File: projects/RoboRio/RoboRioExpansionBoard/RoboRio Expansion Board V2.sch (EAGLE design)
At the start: 94 parts, among them IC1 FT232RL, J1 RRINTERFACE-FEMALE, J2 MICROSD, Q1 5.0 MHz, T1 NPN-SOT416, T2 NPN-SOT416, U1 P8X32A-Q44, U2 24LC256ST, U4 MC1525TO, U6 RT9193-33GB, U7 RT9193-33GB

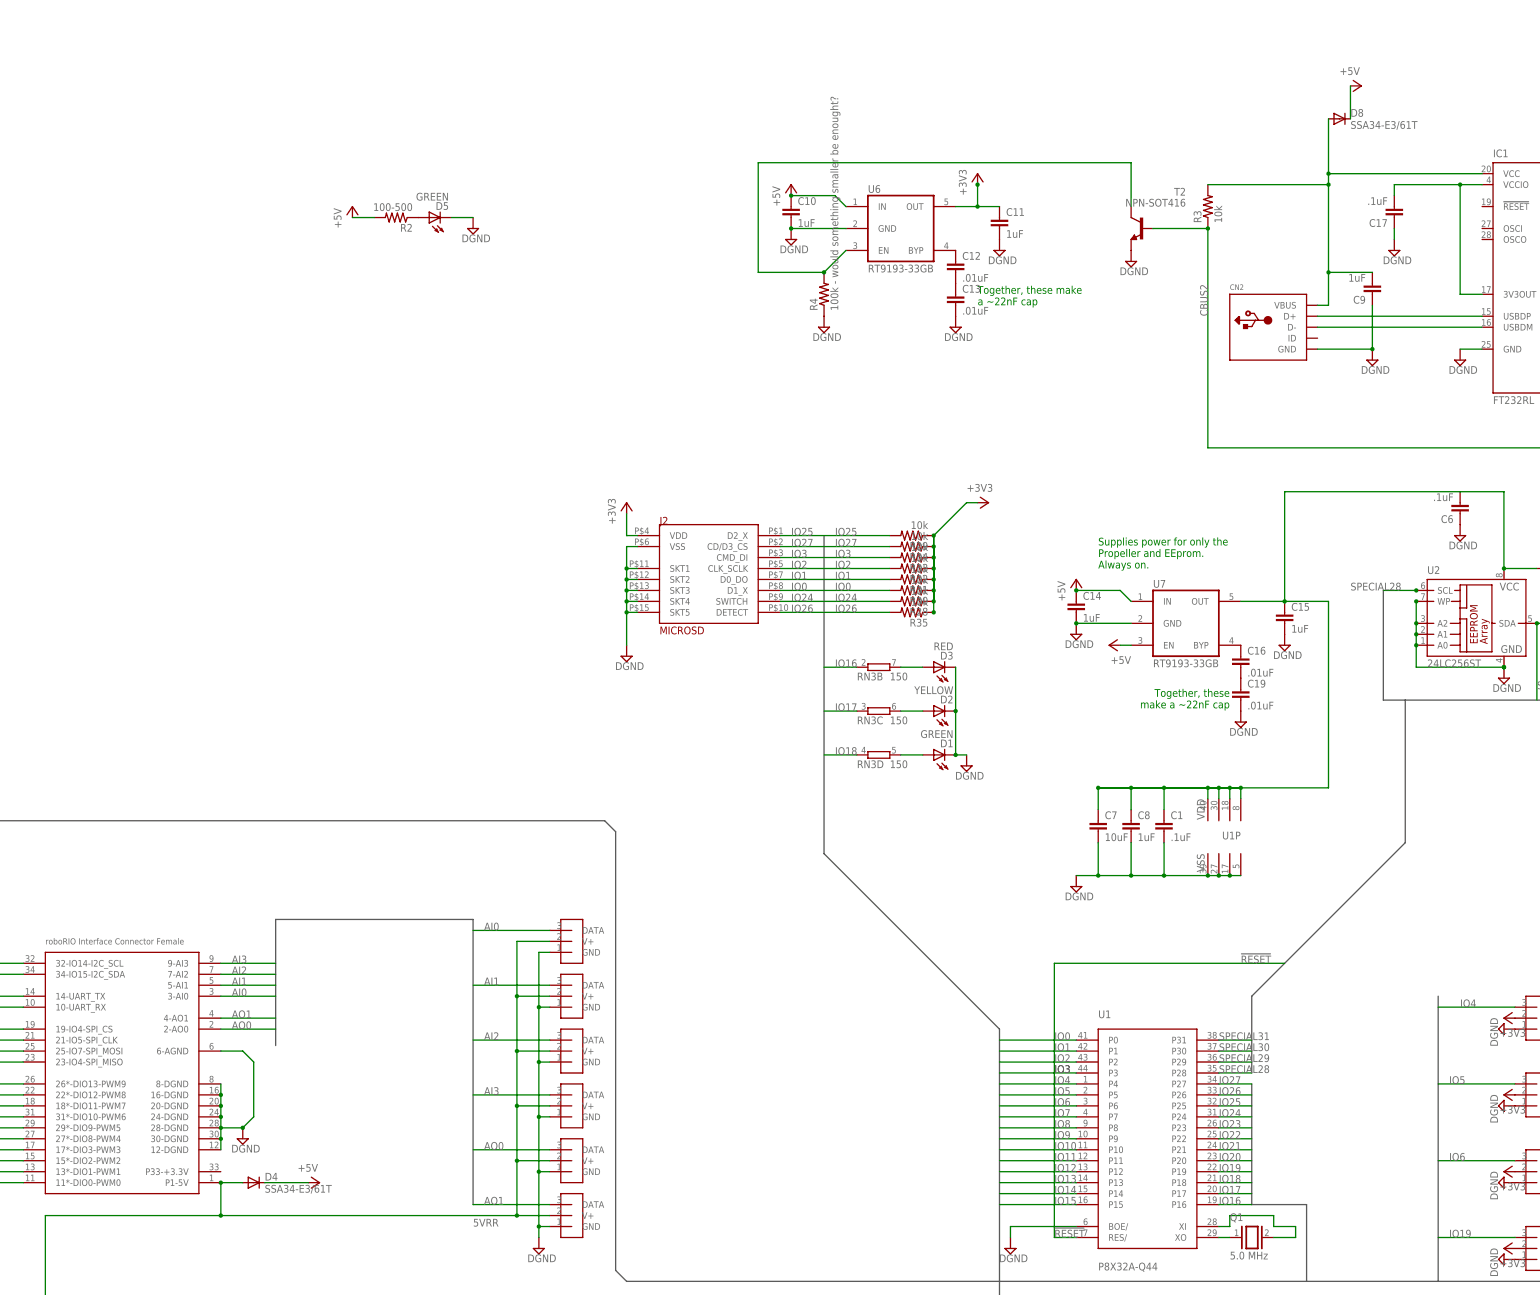
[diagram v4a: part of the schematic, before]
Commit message: Figured out power supply circuit
I think. We need to do a simulation on this!
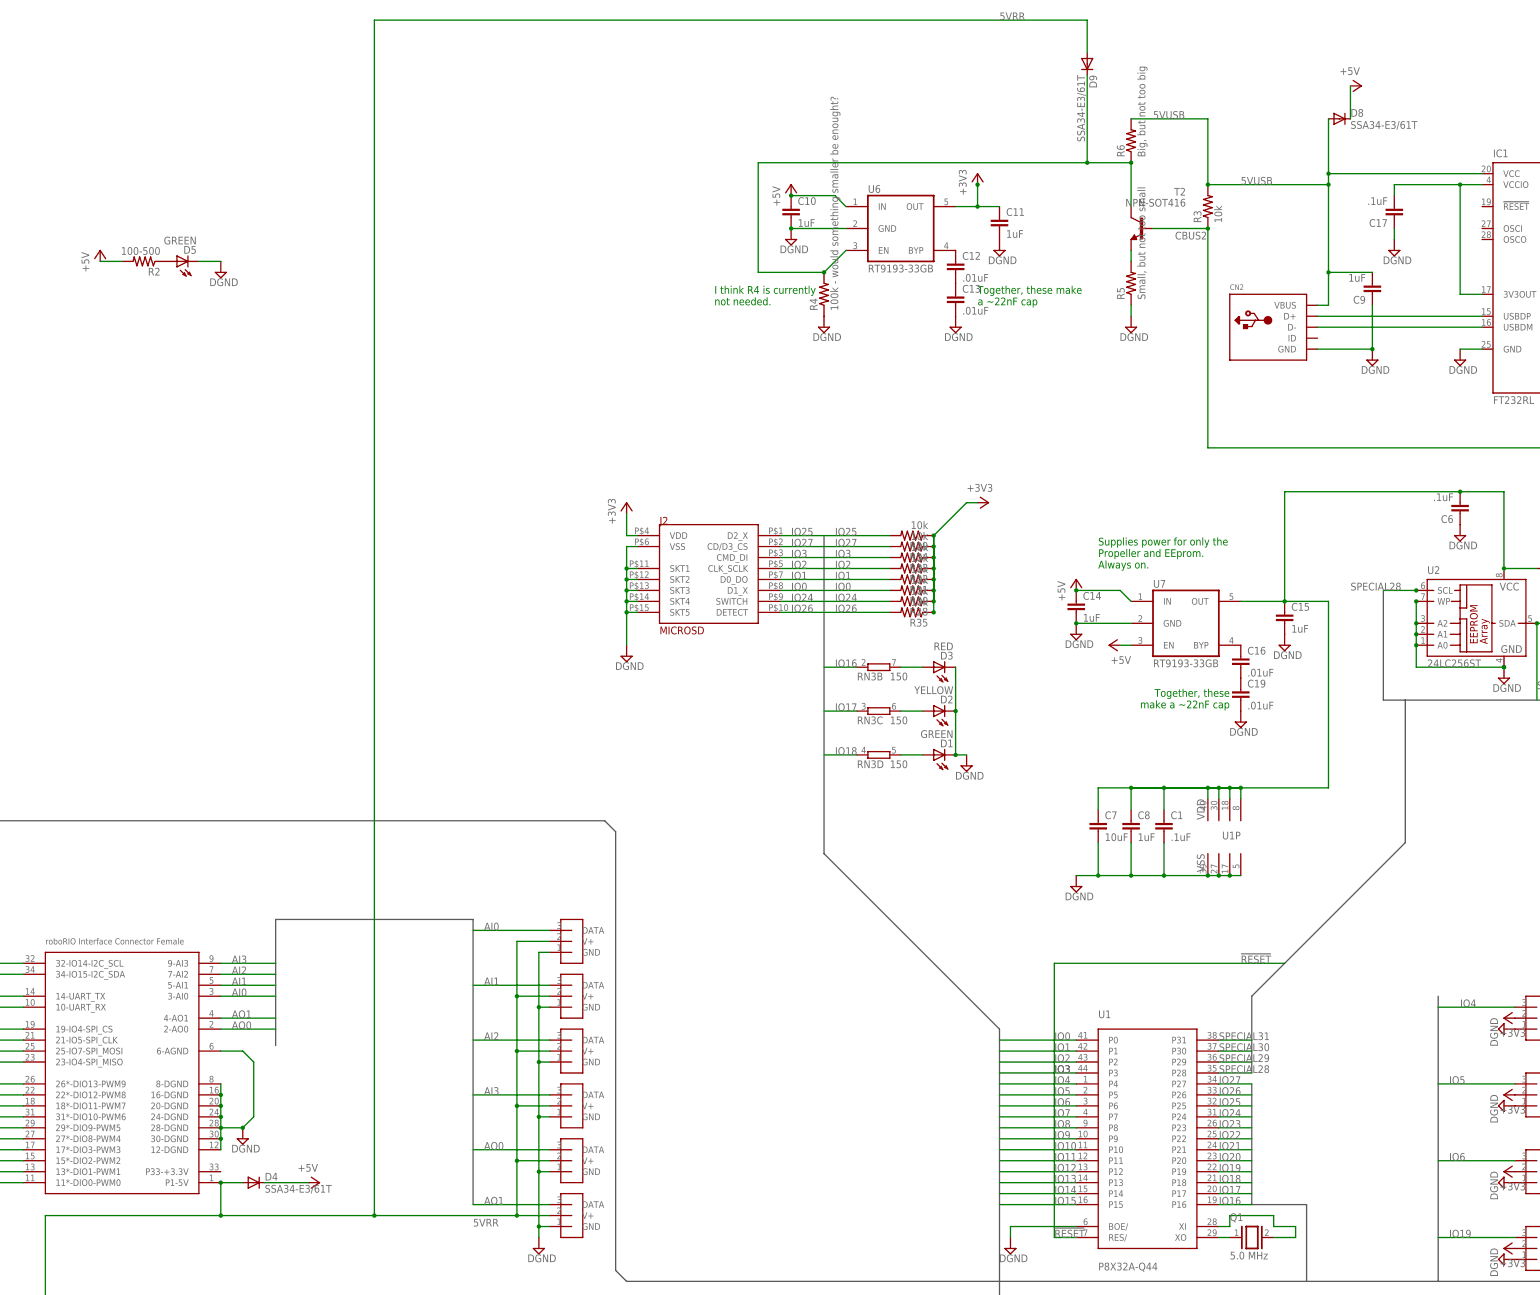
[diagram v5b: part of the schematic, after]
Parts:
- added D9: SSA34-E3/61T, diode:DIODE-DO-214AC
- added R5: Small, but not too small, resistor:R-US_R0603
- added R6: Big, but not too big, resistor:R-US_R0603
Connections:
- new net N$5: R5.2, T2.E
- net 5VRR: now also D9.A
- net 5VUSB: now also R6.2
- net DGND: now also R5.1; no longer T2.E
- net N$25: now also D9.C, R6.1
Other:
- note added: "I think R4 is currently not needed."
- moved on the sheet: D5, R2
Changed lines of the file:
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@@
 <part name="R4" library="resistor" deviceset="R-US_" device="R0603" value="100k - would something smaller be enought?"/>
 <part name="SUPPLY52" library="supply2" deviceset="DGND" device=""/>
+<part name="R5" library="resistor" deviceset="R-US_" device="R0603" value="Small, but not too small"/>
+<part name="D9" library="diode" deviceset="DIODE-" device="DO-214AC" value="SSA34-E3/61T"/>
+<part name="R6" library="resistor" deviceset="R-US_" device="R0603" value="Big, but not too big"/>
 </parts>
 <sheets>
@@
 Propeller and EEprom.
 Always on.</text>
+<text x="-66.04" y="226.06" size="1.778" layer="91">I think R4 is currently
+not needed.</text>
 </plain>
 <instances>
@@
 <instance part="P+13" gate="1" x="254" y="-95.25" rot="R180"/>
 <instance part="P+14" gate="1" x="256.54" y="-72.39" rot="R180"/>
-<instance part="D5" gate="G$1" x="-132.08" y="246.38" rot="R90"/>
-<instance part="SUPPLY39" gate="G$1" x="-121.92" y="243.84"/>
+<instance part="D5" gate="G$1" x="-190.5" y="236.22" rot="R90"/>
+<instance part="SUPPLY39" gate="G$1" x="-180.34" y="233.68"/>
 <instance part="+3V7" gate="G$1" x="-5.08" y="256.54"/>
-<instance part="P+16" gate="1" x="-149.86" y="248.92"/>
+<instance part="P+16" gate="1" x="-208.28" y="238.76"/>
 <instance part="+3V3" gate="G$1" x="116.84" y="60.96" rot="R90"/>
 <instance part="SUPPLY5" gate="G$1" x="116.84" y="58.42" rot="R270"/>
@@
 <instance part="U$36" gate="G$1" x="241.3" y="60.96" rot="R180"/>
 <instance part="U$37" gate="G$1" x="96.52" y="-27.94" rot="R180"/>
-<instance part="R2" gate="G$1" x="-139.7" y="246.38" rot="R180"/>
+<instance part="R2" gate="G$1" x="-198.12" y="236.22" rot="R180"/>
 <instance part="U6" gate="G$1" x="-22.86" y="243.84"/>
 <instance part="C10" gate="G$1" x="-48.26" y="248.92"/>
@@
 <instance part="P+4" gate="1" x="83.82" y="276.86" rot="R270"/>
 <instance part="T2" gate="G$1" x="33.02" y="243.84" rot="MR0"/>
-<instance part="SUPPLY51" gate="G$1" x="30.48" y="236.22"/>
+<instance part="SUPPLY51" gate="G$1" x="30.48" y="220.98"/>
 <instance part="R3" gate="G$1" x="48.26" y="248.92" rot="R90"/>
 <instance part="R4" gate="G$1" x="-40.64" y="228.6" rot="R90"/>
 <instance part="SUPPLY52" gate="G$1" x="-40.64" y="220.98"/>
+<instance part="R5" gate="G$1" x="30.48" y="231.14" rot="R90"/>
+<instance part="D9" gate="G$1" x="20.32" y="281.94" rot="R270"/>
+<instance part="R6" gate="G$1" x="30.48" y="264.16" rot="R90"/>
 </instances>
 <busses>
@@
 <segment>
 <pinref part="P+16" gate="1" pin="+5V"/>
-<wire x1="-149.86" y1="246.38" x2="-144.78" y2="246.38" width="0.1524" layer="91"/>
+<wire x1="-208.28" y1="236.22" x2="-203.2" y2="236.22" width="0.1524" layer="91"/>
 <pinref part="R2" gate="G$1" pin="2"/>
 </segment>
@@
 <pinref part="D5" gate="G$1" pin="C"/>
 <pinref part="SUPPLY39" gate="G$1" pin="DGND"/>
-<wire x1="-121.92" y1="246.38" x2="-127" y2="246.38" width="0.1524" layer="91"/>
+<wire x1="-180.34" y1="236.22" x2="-185.42" y2="236.22" width="0.1524" layer="91"/>
 </segment>
 <segment>
@@
 </segment>
 <segment>
-<pinref part="T2" gate="G$1" pin="E"/>
-<pinref part="SUPPLY51" gate="G$1" pin="DGND"/>
-</segment>
-<segment>
 <pinref part="R4" gate="G$1" pin="1"/>
 <pinref part="SUPPLY52" gate="G$1" pin="DGND"/>
@@
 <pinref part="SUPPLY40" gate="G$1" pin="DGND"/>
 <wire x1="139.7" y1="208.28" x2="144.78" y2="208.28" width="0.1524" layer="91"/>
+</segment>
+<segment>
+<pinref part="SUPPLY51" gate="G$1" pin="DGND"/>
+<pinref part="R5" gate="G$1" pin="1"/>
+<wire x1="30.48" y1="223.52" x2="30.48" y2="226.06" width="0.1524" layer="91"/>
 </segment>
 </net>
@@
 <wire x1="76.2" y1="254" x2="48.26" y2="254" width="0.1524" layer="91"/>
 <junction x="76.2" y="254"/>
+<pinref part="R6" gate="G$1" pin="2"/>
+<wire x1="30.48" y1="269.24" x2="48.26" y2="269.24" width="0.1524" layer="91"/>
+<wire x1="48.26" y1="269.24" x2="48.26" y2="254" width="0.1524" layer="91"/>
+<junction x="48.26" y="254"/>
+<label x="55.88" y="254" size="1.778" layer="95"/>
+<label x="35.56" y="269.24" size="1.778" layer="95"/>
 </segment>
 </net>
@@
 <wire x1="48.26" y1="114.3" x2="50.8" y2="114.3" width="0.1524" layer="91"/>
 <wire x1="50.8" y1="114.3" x2="53.34" y2="114.3" width="0.1524" layer="91"/>
-<wire x1="55.88" y1="114.3" x2="22.86" y2="114.3" width="0.1524" layer="91"/>
+<wire x1="55.88" y1="114.3" x2="30.48" y2="114.3" width="0.1524" layer="91"/>
 <wire x1="50.8" y1="111.76" x2="50.8" y2="114.3" width="0.1524" layer="91"/>
 <junction x="50.8" y="114.3"/>
@@
 <pinref part="U1" gate="P" pin="VDD@1"/>
 <wire x1="55.88" y1="111.76" x2="55.88" y2="114.3" width="0.1524" layer="91"/>
-<junction x="22.86" y="114.3"/>
 <wire x1="55.88" y1="114.3" x2="76.2" y2="114.3" width="0.1524" layer="91"/>
 <wire x1="76.2" y1="114.3" x2="76.2" y2="157.48" width="0.1524" layer="91"/>
 <wire x1="76.2" y1="157.48" x2="66.04" y2="157.48" width="0.1524" layer="91"/>
 <junction x="66.04" y="157.48"/>
+<junction x="106.68" y="182.88"/>
 </segment>
 </net>
@@
 <pinref part="U$16" gate="G$1" pin="V+"/>
 <wire x1="-111.76" y1="15.24" x2="-104.14" y2="15.24" width="0.1524" layer="91"/>
-<wire x1="-180.34" y1="15.24" x2="-111.76" y2="15.24" width="0.1524" layer="91"/>
+<wire x1="-180.34" y1="15.24" x2="-144.78" y2="15.24" width="0.1524" layer="91"/>
 <junction x="-111.76" y="15.24"/>
 <junction x="-180.34" y="15.24"/>
 <label x="-121.92" y="12.7" size="1.778" layer="95"/>
 <label x="-254" y="-50.8" size="1.778" layer="95"/>
+<wire x1="-144.78" y1="15.24" x2="-111.76" y2="15.24" width="0.1524" layer="91"/>
+<wire x1="-144.78" y1="15.24" x2="-144.78" y2="292.1" width="0.1524" layer="91"/>
+<wire x1="-144.78" y1="292.1" x2="20.32" y2="292.1" width="0.1524" layer="91"/>
+<wire x1="20.32" y1="292.1" x2="20.32" y2="284.48" width="0.1524" layer="91"/>
+<label x="0" y="292.1" size="1.778" layer="95"/>
+<pinref part="D9" gate="G$1" pin="A"/>
+<junction x="-144.78" y="15.24"/>
 </segment>
 </net>
@@
 <wire x1="-40.64" y1="233.68" x2="-55.88" y2="233.68" width="0.1524" layer="91"/>
 <wire x1="-55.88" y1="233.68" x2="-55.88" y2="259.08" width="0.1524" layer="91"/>
-<wire x1="-55.88" y1="259.08" x2="30.48" y2="259.08" width="0.1524" layer="91"/>
+<wire x1="-55.88" y1="259.08" x2="20.32" y2="259.08" width="0.1524" layer="91"/>
 <pinref part="T2" gate="G$1" pin="C"/>
+<wire x1="20.32" y1="259.08" x2="30.48" y2="259.08" width="0.1524" layer="91"/>
 <wire x1="30.48" y1="259.08" x2="30.48" y2="248.92" width="0.1524" layer="91"/>
 <pinref part="R4" gate="G$1" pin="2"/>
 <junction x="-40.64" y="233.68"/>
+<pinref part="D9" gate="G$1" pin="C"/>
+<wire x1="20.32" y1="279.4" x2="20.32" y2="259.08" width="0.1524" layer="91"/>
+<pinref part="R6" gate="G$1" pin="1"/>
+<junction x="30.48" y="259.08"/>
+<junction x="20.32" y="259.08"/>
 </segment>
 </net>
@@
 <pinref part="R3" gate="G$1" pin="1"/>
 <junction x="48.26" y="243.84"/>
-<label x="48.26" y="223.52" size="1.778" layer="95" rot="R90"/>
-</segment>
-</net>
+<label x="40.64" y="241.3" size="1.778" layer="95"/>
+</segment>
+</net>
+<net name="N$5" class="0">
+<segment>
+<pinref part="T2" gate="G$1" pin="E"/>
+<pinref part="R5" gate="G$1" pin="2"/>
+<wire x1="30.48" y1="236.22" x2="30.48" y2="238.76" width="0.1524" layer="91"/>
+</segment>
+</net>

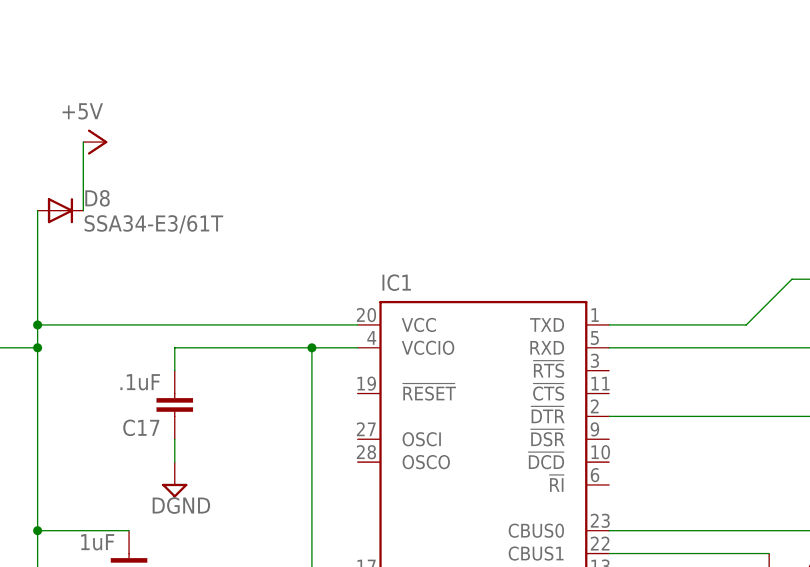
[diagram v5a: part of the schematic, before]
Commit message: renamed FT232R to U3
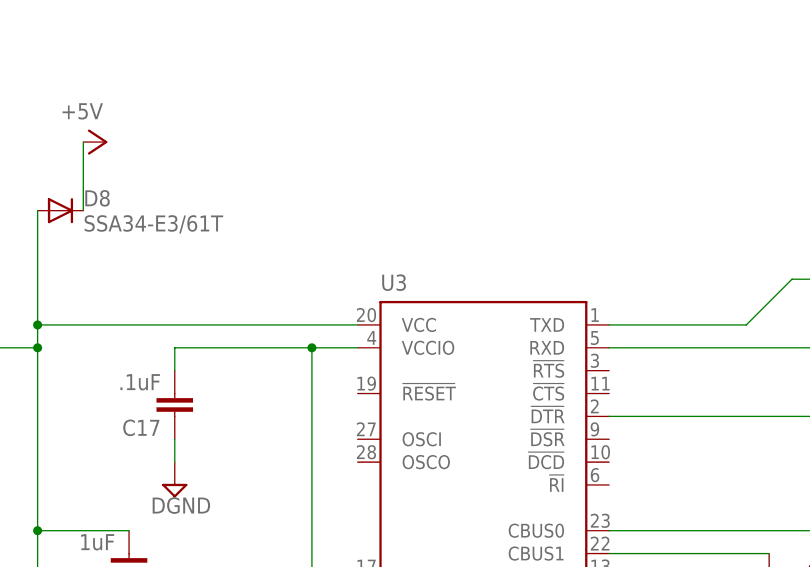
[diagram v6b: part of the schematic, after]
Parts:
- renumbered IC1 to U3
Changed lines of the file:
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@@
 <part name="D4" library="diode" deviceset="DIODE-" device="DO-214AC" value="SSA34-E3/61T"/>
 <part name="P+3" library="supply1" deviceset="+5V" device=""/>
-<part name="IC1" library="ftdichip" deviceset="FT232R" device="L"/>
+<part name="U3" library="ftdichip" deviceset="FT232R" device="L"/>
 <part name="SUPPLY40" library="supply2" deviceset="DGND" device=""/>
 <part name="D8" library="diode" deviceset="DIODE-" device="DO-214AC" value="SSA34-E3/61T"/>
@@
 <instance part="D4" gate="G$1" x="-172.72" y="22.86"/>
 <instance part="P+3" gate="1" x="-157.48" y="22.86" rot="R270"/>
-<instance part="IC1" gate="1" x="124.46" y="233.68"/>
+<instance part="U3" gate="1" x="124.46" y="233.68"/>
 <instance part="SUPPLY40" gate="G$1" x="144.78" y="205.74"/>
 <instance part="D8" gate="G$1" x="78.74" y="269.24"/>
@@
 </segment>
 <segment>
-<pinref part="IC1" gate="1" pin="GND@A"/>
+<pinref part="U3" gate="1" pin="GND@A"/>
 <pinref part="SUPPLY20" gate="G$1" pin="DGND"/>
 <wire x1="106.68" y1="215.9" x2="111.76" y2="215.9" width="0.1524" layer="91"/>
@@
 </segment>
 <segment>
-<pinref part="IC1" gate="1" pin="GND@1"/>
-<pinref part="IC1" gate="1" pin="GND@2"/>
+<pinref part="U3" gate="1" pin="GND@1"/>
+<pinref part="U3" gate="1" pin="GND@2"/>
 <wire x1="139.7" y1="208.28" x2="139.7" y2="210.82" width="0.1524" layer="91"/>
-<pinref part="IC1" gate="1" pin="GND"/>
+<pinref part="U3" gate="1" pin="GND"/>
 <wire x1="139.7" y1="213.36" x2="139.7" y2="210.82" width="0.1524" layer="91"/>
 <junction x="139.7" y="210.82"/>
 <junction x="139.7" y="213.36"/>
-<pinref part="IC1" gate="1" pin="TEST"/>
+<pinref part="U3" gate="1" pin="TEST"/>
 <wire x1="139.7" y1="213.36" x2="139.7" y2="218.44" width="0.1524" layer="91"/>
 <junction x="139.7" y="208.28"/>
@@
 <wire x1="165.1" y1="254" x2="139.7" y2="254" width="0.1524" layer="91"/>
 <pinref part="RN1" gate="B" pin="1"/>
-<pinref part="IC1" gate="1" pin="RXD"/>
+<pinref part="U3" gate="1" pin="RXD"/>
 </segment>
 </net>
@@
 <wire x1="160.02" y1="261.62" x2="165.1" y2="261.62" width="0.1524" layer="91"/>
 <pinref part="RN1" gate="C" pin="1"/>
-<pinref part="IC1" gate="1" pin="TXD"/>
+<pinref part="U3" gate="1" pin="TXD"/>
 <wire x1="154.94" y1="256.54" x2="139.7" y2="256.54" width="0.1524" layer="91"/>
 </segment>
@@
 <pinref part="CN2" gate="G$1" pin="D-"/>
 <wire x1="73.66" y1="220.98" x2="111.76" y2="220.98" width="0.1524" layer="91"/>
-<pinref part="IC1" gate="1" pin="USBDM"/>
+<pinref part="U3" gate="1" pin="USBDM"/>
 </segment>
 </net>
@@
 <pinref part="CN2" gate="G$1" pin="D+"/>
 <wire x1="73.66" y1="223.52" x2="111.76" y2="223.52" width="0.1524" layer="91"/>
-<pinref part="IC1" gate="1" pin="USBDP"/>
+<pinref part="U3" gate="1" pin="USBDP"/>
 </segment>
 </net>
@@
 <pinref part="C18" gate="G$1" pin="1"/>
 <wire x1="165.1" y1="246.38" x2="139.7" y2="246.38" width="0.1524" layer="91"/>
-<pinref part="IC1" gate="1" pin="!DTR"/>
+<pinref part="U3" gate="1" pin="!DTR"/>
 </segment>
 </net>
@@
 <wire x1="86.36" y1="233.68" x2="76.2" y2="233.68" width="0.1524" layer="91"/>
 <junction x="76.2" y="233.68"/>
-<pinref part="IC1" gate="1" pin="VCC"/>
+<pinref part="U3" gate="1" pin="VCC"/>
 <pinref part="D8" gate="G$1" pin="A"/>
 <wire x1="76.2" y1="269.24" x2="76.2" y2="256.54" width="0.1524" layer="91"/>
@@
 <pinref part="C17" gate="G$1" pin="2"/>
 <wire x1="91.44" y1="251.46" x2="91.44" y2="254" width="0.1524" layer="91"/>
-<pinref part="IC1" gate="1" pin="VCCIO"/>
+<pinref part="U3" gate="1" pin="VCCIO"/>
 <wire x1="91.44" y1="254" x2="106.68" y2="254" width="0.1524" layer="91"/>
-<pinref part="IC1" gate="1" pin="3V3OUT"/>
+<pinref part="U3" gate="1" pin="3V3OUT"/>
 <wire x1="106.68" y1="254" x2="111.76" y2="254" width="0.1524" layer="91"/>
 <wire x1="111.76" y1="228.6" x2="106.68" y2="228.6" width="0.1524" layer="91"/>
@@
 <net name="N$27" class="0">
 <segment>
-<pinref part="IC1" gate="1" pin="CBUS0"/>
+<pinref part="U3" gate="1" pin="CBUS0"/>
 <pinref part="D7" gate="G$1" pin="A"/>
 <wire x1="165.1" y1="233.68" x2="139.7" y2="233.68" width="0.1524" layer="91"/>
@@
 <net name="N$28" class="0">
 <segment>
-<pinref part="IC1" gate="1" pin="CBUS1"/>
+<pinref part="U3" gate="1" pin="CBUS1"/>
 <pinref part="D6" gate="G$1" pin="A"/>
 <wire x1="157.48" y1="231.14" x2="139.7" y2="231.14" width="0.1524" layer="91"/>
@@
 <net name="CBUS2" class="0">
 <segment>
-<pinref part="IC1" gate="1" pin="CBUS2"/>
+<pinref part="U3" gate="1" pin="CBUS2"/>
 <wire x1="139.7" y1="228.6" x2="149.86" y2="228.6" width="0.1524" layer="91"/>
 <wire x1="149.86" y1="228.6" x2="149.86" y2="193.04" width="0.1524" layer="91"/>
